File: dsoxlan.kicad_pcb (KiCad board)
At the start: 2 copper layers, 81.3 x 58.4 mm, 11 parts, among them P1 CNT-RJ45, P2 CONN_02X40

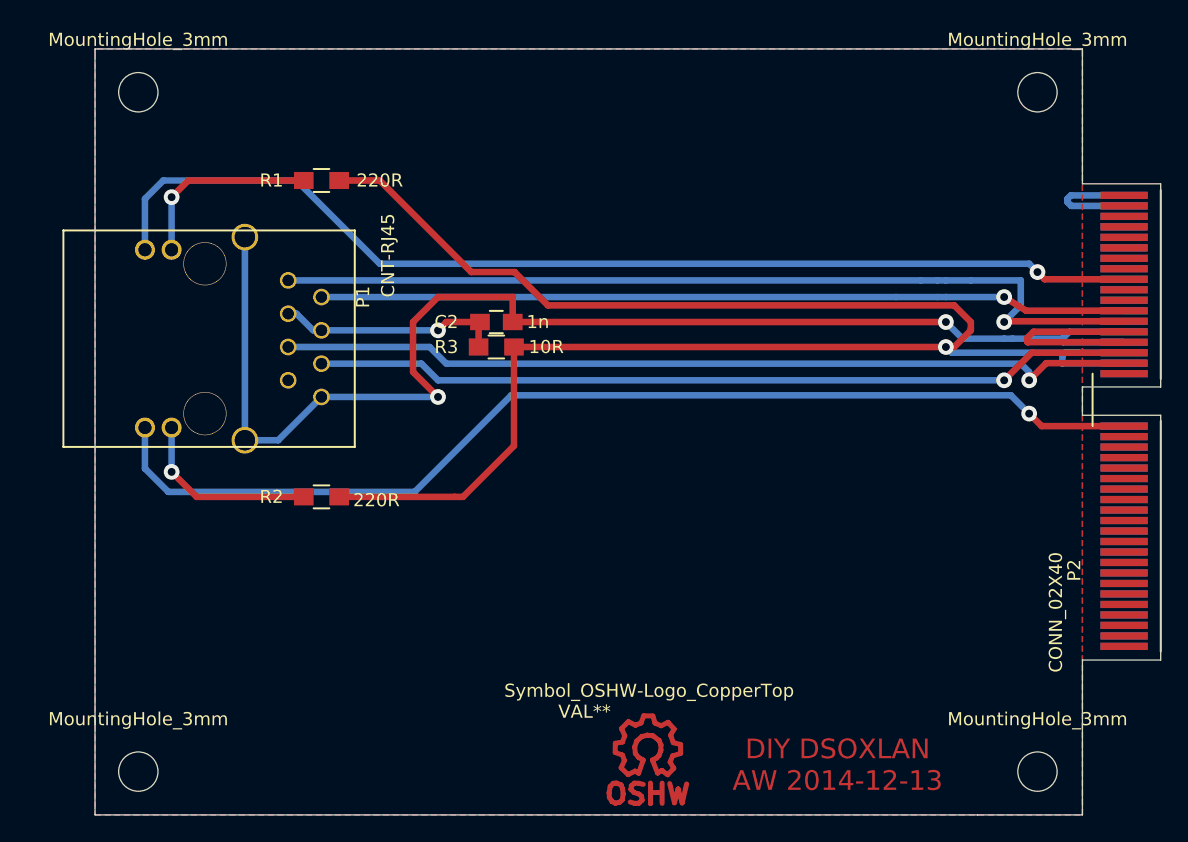
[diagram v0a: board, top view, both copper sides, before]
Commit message: Basic upgrade to Kicad 7+
Symbols had to be recreated because they were not part of
original dataset.

Footprint library now needs to end in .pretty

Still many DRC warnings, but the basic result ought to be
the same as before now.
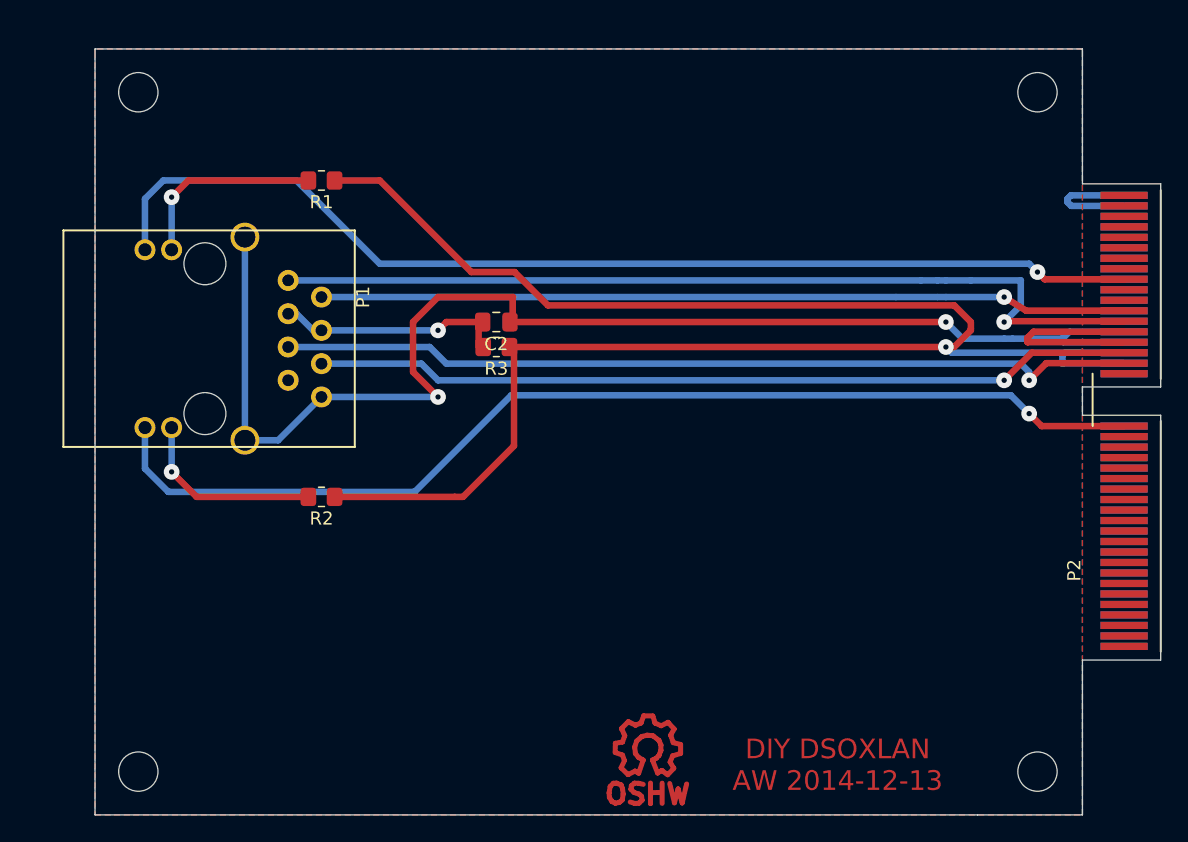
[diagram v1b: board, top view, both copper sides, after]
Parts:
- C2: footprint Capacitors_SMD:C_0805_HandSoldering -> Capacitor_SMD:C_0805_2012Metric_Pad1.18x1.45mm_HandSolder
- P1: footprint awallin:ETH-MAGJACK -> DSOXLAN:ETH-MAGJACK
- P2: footprint awallin:cardedge_40x2 -> DSOXLAN:cardedge_40x2
- R1, R2, R3: footprint Resistors_SMD:R_0805_HandSoldering -> Resistor_SMD:R_0805_2012Metric_Pad1.20x1.40mm_HandSolder
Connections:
- net +3V3 renamed +3.3V
- P1 pad 7: Net-(P1-Pad7) -> unconnected-(P1-Pad7)
- P2 pad 1: Net-(P2-Pad1) -> unconnected-(P2-Pin_1-Pad1)
- P2 pad 10: Net-(P2-Pad10) -> unconnected-(P2-Pin_10-Pad10)
- P2 pad 11: Net-(P2-Pad11) -> unconnected-(P2-Pin_11-Pad11)
- P2 pad 12: Net-(P2-Pad12) -> unconnected-(P2-Pin_12-Pad12)
- P2 pad 13: Net-(P2-Pad13) -> unconnected-(P2-Pin_13-Pad13)
- P2 pad 14: Net-(P2-Pad14) -> unconnected-(P2-Pin_14-Pad14)
- P2 pad 15: Net-(P2-Pad15) -> unconnected-(P2-Pin_15-Pad15)
- P2 pad 16: Net-(P2-Pad16) -> unconnected-(P2-Pin_16-Pad16)
- P2 pad 17: Net-(P2-Pad17) -> unconnected-(P2-Pin_17-Pad17)
- P2 pad 18: Net-(P2-Pad18) -> unconnected-(P2-Pin_18-Pad18)
- P2 pad 19: Net-(P2-Pad19) -> unconnected-(P2-Pin_19-Pad19)
- P2 pad 2: Net-(P2-Pad2) -> unconnected-(P2-Pin_2-Pad2)
- P2 pad 20: Net-(P2-Pad20) -> unconnected-(P2-Pin_20-Pad20)
- P2 pad 21: Net-(P2-Pad21) -> unconnected-(P2-Pin_21-Pad21)
- P2 pad 22: Net-(P2-Pad22) -> unconnected-(P2-Pin_22-Pad22)
- P2 pad 23: Net-(P2-Pad23) -> unconnected-(P2-Pin_23-Pad23)
- P2 pad 24: Net-(P2-Pad24) -> unconnected-(P2-Pin_24-Pad24)
- P2 pad 25: Net-(P2-Pad25) -> unconnected-(P2-Pin_25-Pad25)
- P2 pad 26: Net-(P2-Pad26) -> unconnected-(P2-Pin_26-Pad26)
- P2 pad 27: Net-(P2-Pad27) -> unconnected-(P2-Pin_27-Pad27)
- P2 pad 28: Net-(P2-Pad28) -> unconnected-(P2-Pin_28-Pad28)
- P2 pad 29: Net-(P2-Pad29) -> unconnected-(P2-Pin_29-Pad29)
- P2 pad 3: Net-(P2-Pad3) -> unconnected-(P2-Pin_3-Pad3)
- P2 pad 30: Net-(P2-Pad30) -> unconnected-(P2-Pin_30-Pad30)
- P2 pad 31: Net-(P2-Pad31) -> unconnected-(P2-Pin_31-Pad31)
- P2 pad 32: Net-(P2-Pad32) -> unconnected-(P2-Pin_32-Pad32)
- P2 pad 33: Net-(P2-Pad33) -> unconnected-(P2-Pin_33-Pad33)
- P2 pad 34: Net-(P2-Pad34) -> unconnected-(P2-Pin_34-Pad34)
- P2 pad 35: Net-(P2-Pad35) -> unconnected-(P2-Pin_35-Pad35)
- P2 pad 36: Net-(P2-Pad36) -> unconnected-(P2-Pin_36-Pad36)
- P2 pad 37: Net-(P2-Pad37) -> unconnected-(P2-Pin_37-Pad37)
- P2 pad 38: Net-(P2-Pad38) -> unconnected-(P2-Pin_38-Pad38)
- P2 pad 39: Net-(P2-Pad39) -> unconnected-(P2-Pin_39-Pad39)
- P2 pad 4: Net-(P2-Pad4) -> unconnected-(P2-Pin_4-Pad4)
- P2 pad 40: Net-(P2-Pad40) -> unconnected-(P2-Pin_40-Pad40)
- P2 pad 41: Net-(P2-Pad41) -> unconnected-(P2-Pin_41-Pad41)
- P2 pad 42: Net-(P2-Pad42) -> unconnected-(P2-Pin_42-Pad42)
- P2 pad 44: Net-(P2-Pad44) -> unconnected-(P2-Pin_44-Pad44)
- P2 pad 45: Net-(P2-Pad45) -> unconnected-(P2-Pin_45-Pad45)
- P2 pad 46: Net-(P2-Pad46) -> unconnected-(P2-Pin_46-Pad46)
- P2 pad 5: Net-(P2-Pad5) -> unconnected-(P2-Pin_5-Pad5)
- P2 pad 56: Net-(P2-Pad56) -> unconnected-(P2-Pin_56-Pad56)
- P2 pad 58: Net-(P2-Pad58) -> unconnected-(P2-Pin_58-Pad58)
- P2 pad 59: Net-(P2-Pad59) -> unconnected-(P2-Pin_59-Pad59)
- P2 pad 6: Net-(P2-Pad6) -> unconnected-(P2-Pin_6-Pad6)
- P2 pad 60: Net-(P2-Pad60) -> unconnected-(P2-Pin_60-Pad60)
- P2 pad 61: Net-(P2-Pad61) -> unconnected-(P2-Pin_61-Pad61)
- P2 pad 62: Net-(P2-Pad62) -> unconnected-(P2-Pin_62-Pad62)
- P2 pad 64: Net-(P2-Pad64) -> unconnected-(P2-Pin_64-Pad64)
- P2 pad 65: Net-(P2-Pad65) -> unconnected-(P2-Pin_65-Pad65)
- P2 pad 66: Net-(P2-Pad66) -> unconnected-(P2-Pin_66-Pad66)
- P2 pad 67: Net-(P2-Pad67) -> unconnected-(P2-Pin_67-Pad67)
- P2 pad 68: Net-(P2-Pad68) -> unconnected-(P2-Pin_68-Pad68)
- P2 pad 69: Net-(P2-Pad69) -> unconnected-(P2-Pin_69-Pad69)
- P2 pad 7: Net-(P2-Pad7) -> unconnected-(P2-Pin_7-Pad7)
- P2 pad 70: Net-(P2-Pad70) -> unconnected-(P2-Pin_70-Pad70)
- P2 pad 71: Net-(P2-Pad71) -> unconnected-(P2-Pin_71-Pad71)
- P2 pad 72: Net-(P2-Pad72) -> unconnected-(P2-Pin_72-Pad72)
- P2 pad 73: Net-(P2-Pad73) -> unconnected-(P2-Pin_73-Pad73)
- P2 pad 74: Net-(P2-Pad74) -> unconnected-(P2-Pin_74-Pad74)
- P2 pad 75: Net-(P2-Pad75) -> unconnected-(P2-Pin_75-Pad75)
- P2 pad 76: Net-(P2-Pad76) -> unconnected-(P2-Pin_76-Pad76)
- P2 pad 77: Net-(P2-Pad77) -> unconnected-(P2-Pin_77-Pad77)
- P2 pad 79: Net-(P2-Pad79) -> unconnected-(P2-Pin_79-Pad79)
- P2 pad 8: Net-(P2-Pad8) -> unconnected-(P2-Pin_8-Pad8)
- P2 pad 9: Net-(P2-Pad9) -> unconnected-(P2-Pin_9-Pad9)
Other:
- net class Default removed
